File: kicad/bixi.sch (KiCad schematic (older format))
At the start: 20 parts, among them J1 RJ45, J2 RJ45, J3 RJ45, J4 RJ45, J5 RJ45, J6 RJ45, J7 RJ45, J8 RJ45, U1 Teensy3.6, U2 sn75lbc978, U3 ESP8266

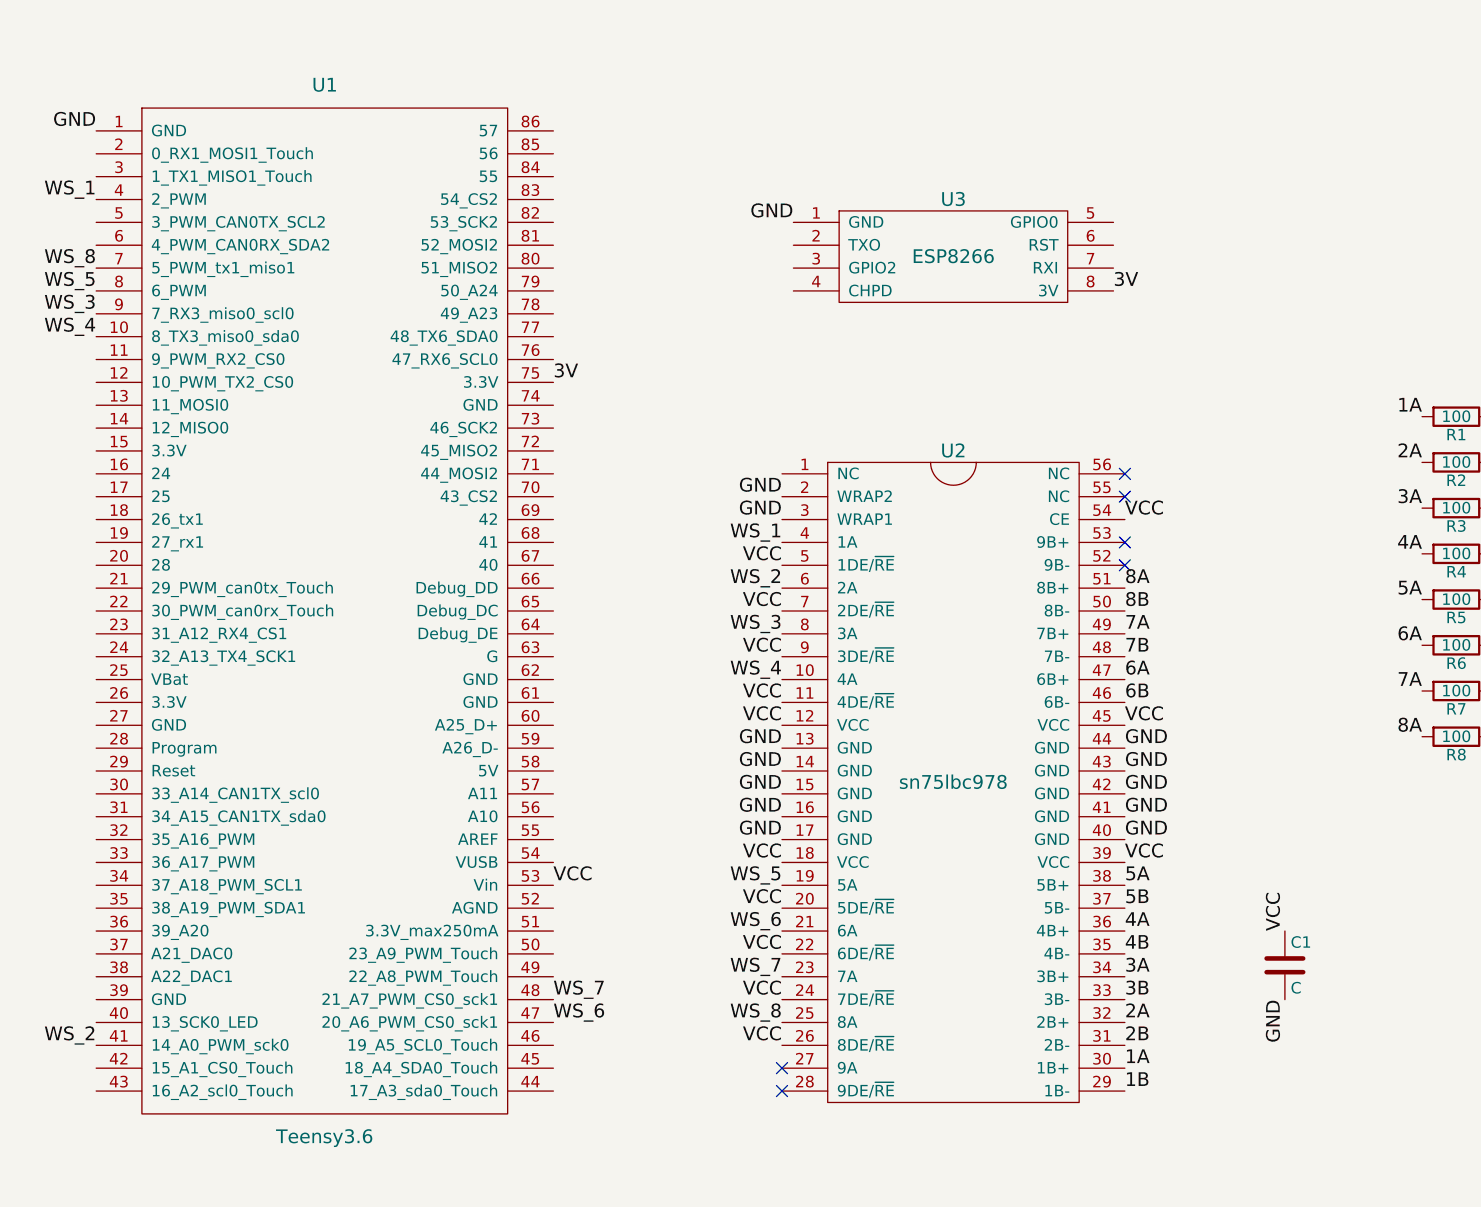
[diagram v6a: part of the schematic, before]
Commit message: v3 boards almost complete. added xcvr breakout, passthrough boards
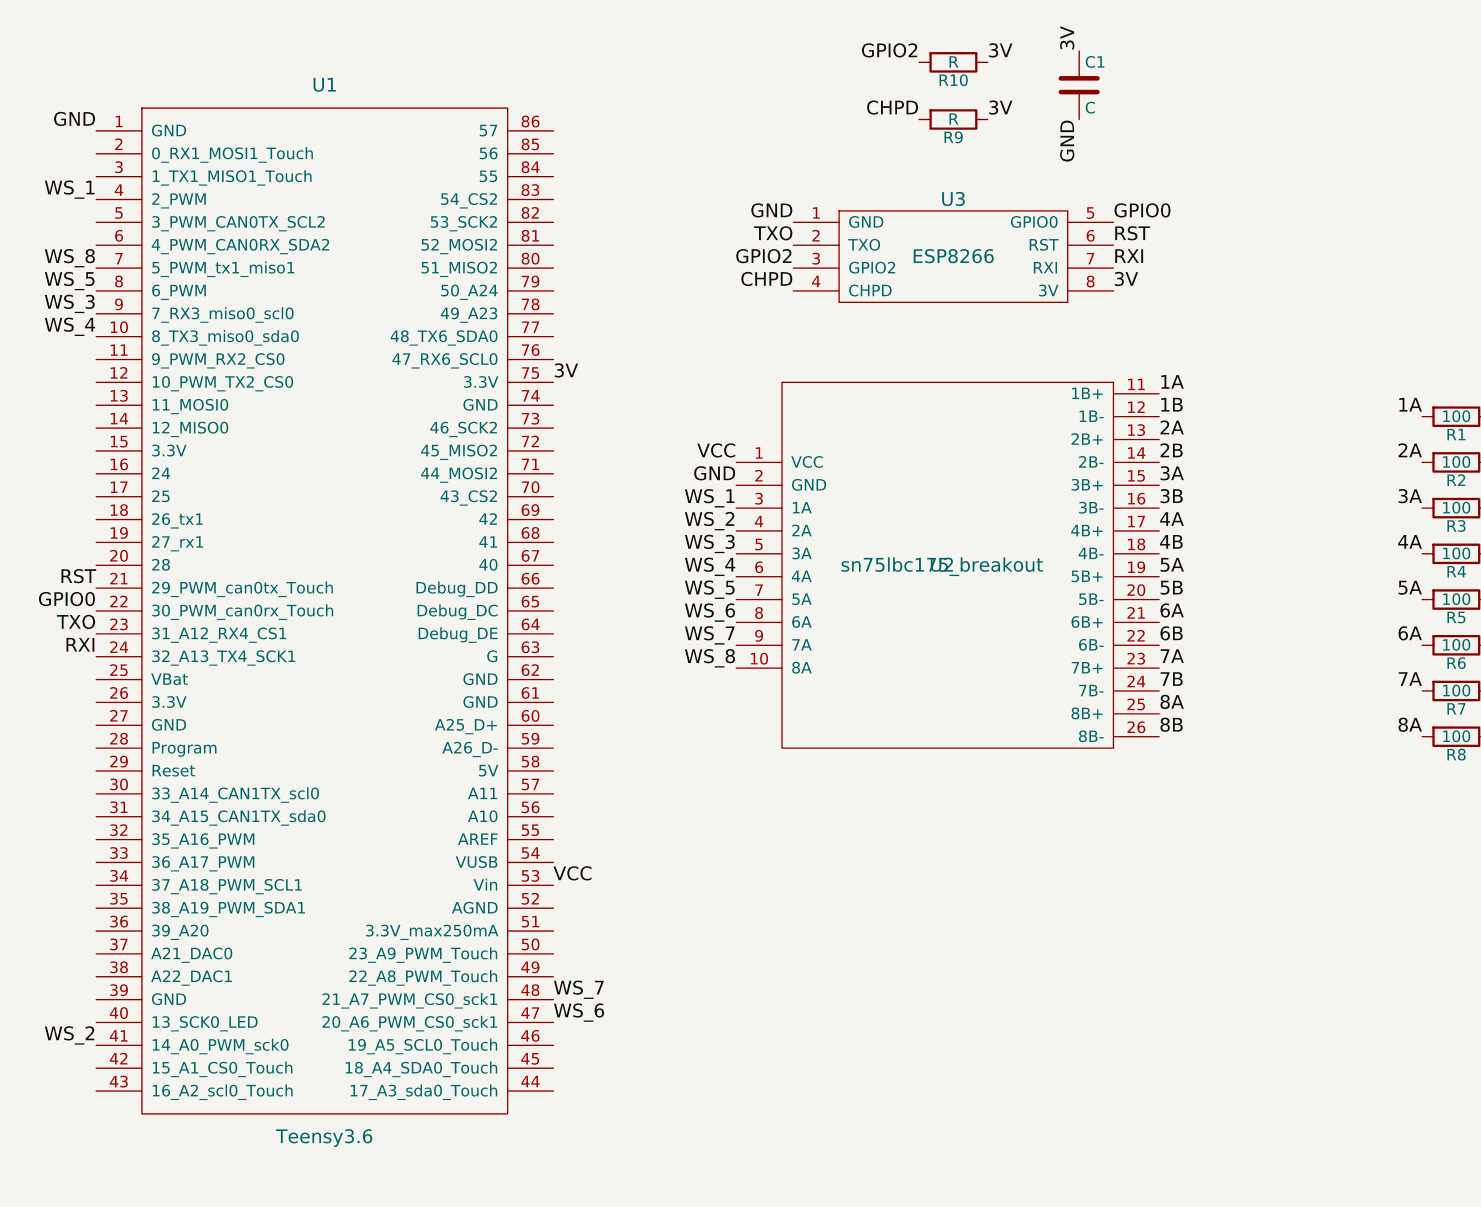
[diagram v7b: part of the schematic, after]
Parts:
- removed U2: sn75lbc978, Housings_SSOP:SSOP-56_7.5x18.5mm_Pitch0.635mm, symbol sn75lbc978
- added R10, R9: R, Resistors_THT:R_Axial_DIN0207_L6.3mm_D2.5mm_P7.62mm_Horizontal, symbol R
- added U2: sn75lbc175_breakout, custom:sn75lbc17f_breakout, symbol sn75lbc175_breakout
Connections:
- net 1A: now also U2.11 (1B+)
- net 1B: now also U2.12 (1B-)
- net 2A: now also U2.13 (2B+)
- net 2B: now also U2.14 (2B-)
- net 3A: now also U2.15 (3B+)
- net 3B: now also U2.16 (3B-)
- net 3V: now also C1.1, R10.1, R9.1
- net 4A: now also U2.17 (4B+)
- net 4B: now also U2.18 (4B-)
- net 5A: now also U2.19 (5B+)
- net 5B: now also U2.20 (5B-)
- net 6A: now also U2.21 (6B+)
- net 6B: now also U2.22 (6B-)
- net 7A: now also U2.23 (7B+)
- net 7B: now also U2.24 (7B-)
- net 8A: now also U2.25 (8B+)
- net 8B: now also U2.26 (8B-)
- net GND: now also U2.2 (GND)
- net VCC: now also U2.1 (VCC); no longer C1.1
- net WS_1: now also U2.3 (1A)
- net WS_2: now also U2.4 (2A)
- net WS_3: now also U2.5 (3A)
- net WS_4: now also U2.6 (4A)
- net WS_5: now also U2.7 (5A)
- net WS_6: now also U2.8 (6A)
- net WS_7: now also U2.9 (7A)
- net WS_8: now also U2.10 (8A)
- net RST: now reaches U1.21 (29_PWM_can0tx_Touch)
- net RST: now also U3.6 (RST)
- net GPIO0: now reaches U1.22 (30_PWM_can0rx_Touch)
- net GPIO0: now also U3.5 (GPIO0)
- net TXO: now reaches U1.23 (31_A12_RX4_CS1)
- net TXO: now also U3.2 (TXO)
- net RXI: now reaches U1.24 (32_A13_TX4_SCK1)
- net RXI: now also U3.7 (RXI)
- net GPIO2: now reaches U3.3 (GPIO2)
- net GPIO2: now also R10.2
- net CHPD: now reaches U3.4 (CHPD)
- net CHPD: now also R9.2
- no-connect marks 6 -> 0
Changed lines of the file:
@@
-	1    0    0    -1
-$EndComp
-$Comp
-L C C1
-U 1 1 58BF16CF
-P 6800 4850
-F 0 "C1" H 6825 4950 50  0000 L CNN
-F 1 "C" H 6825 4750 50  0000 L CNN
-F 2 "Capacitors_THT:C_Disc_D4.7mm_W2.5mm_P5.00mm" H 6838 4700 50  0001 C CNN
-F 3 "" H 6800 4850 50  0000 C CNN
-	1    6800 4850
-	1    0    0    -1
-$EndComp
-$Comp
-L sn75lbc978 U2
-U 1 1 5904BED1
-P 5350 4050
-F 0 "U2" H 5350 5500 60  0000 C CNN
-F 1 "sn75lbc978" H 5350 4050 60  0000 C CNN
-F 2 "Housings_SSOP:SSOP-56_7.5x18.5mm_Pitch0.635mm" H 5350 4050 60  0001 C CNN
-F 3 "" H 5350 4050 60  0001 C CNN
-	1    5350 4050
 	1    0    0    -1
 $EndComp
@@
 Text Label 1600 1500 2    60   ~ 0
 WS_1
-Text Label 4600 3000 2    60   ~ 0
+Text Label 4400 2850 2    60   ~ 0
 WS_1
-Text Label 4600 3200 2    60   ~ 0
+Text Label 4400 2950 2    60   ~ 0
 WS_2
-Text Label 4600 3400 2    60   ~ 0
+Text Label 4400 3050 2    60   ~ 0
 WS_3
-Text Label 4600 3600 2    60   ~ 0
+Text Label 4400 3150 2    60   ~ 0
 WS_4
-Text Label 4600 4500 2    60   ~ 0
+Text Label 4400 3250 2    60   ~ 0
 WS_5
-Text Label 4600 4700 2    60   ~ 0
+Text Label 4400 3350 2    60   ~ 0
 WS_6
-Text Label 4600 4900 2    60   ~ 0
+Text Label 4400 3450 2    60   ~ 0
 WS_7
-Text Label 4600 5100 2    60   ~ 0
+Text Label 4400 3550 2    60   ~ 0
 WS_8
 Text Label 1600 1200 2    60   ~ 0
@@
 Text Label 3600 4500 0    60   ~ 0
 VCC
-Text Label 6100 4400 0    60   ~ 0
+Text Label 4400 2650 2    60   ~ 0
 VCC
-Text Label 6100 3800 0    60   ~ 0
-VCC
-Text Label 4600 3800 2    60   ~ 0
-VCC
-Text Label 4600 4400 2    60   ~ 0
-VCC
-Text Label 4600 3900 2    60   ~ 0
-GND
-Text Label 4600 4000 2    60   ~ 0
-GND
-Text Label 4600 4100 2    60   ~ 0
-GND
-Text Label 4600 4200 2    60   ~ 0
-GND
-Text Label 4600 4300 2    60   ~ 0
-GND
-Text Label 6100 3900 0    60   ~ 0
-GND
-Text Label 6100 4000 0    60   ~ 0
-GND
-Text Label 6100 4100 0    60   ~ 0
-GND
-Text Label 6100 4200 0    60   ~ 0
-GND
-Text Label 6100 4300 0    60   ~ 0
-GND
-Text Label 6100 2900 0    60   ~ 0
-VCC
-Text Label 4600 2800 2    60   ~ 0
-GND
-Text Label 4600 2900 2    60   ~ 0
-GND
-Text Label 4600 3100 2    60   ~ 0
-VCC
-Text Label 4600 3300 2    60   ~ 0
-VCC
-Text Label 4600 3500 2    60   ~ 0
-VCC
-Text Label 4600 3700 2    60   ~ 0
-VCC
-Text Label 4600 4600 2    60   ~ 0
-VCC
-Text Label 4600 4800 2    60   ~ 0
-VCC
-Text Label 4600 5000 2    60   ~ 0
-VCC
-Text Label 4600 5200 2    60   ~ 0
-VCC
-NoConn ~ 4600 5300
-NoConn ~ 4600 5400
-NoConn ~ 6100 2700
-NoConn ~ 6100 2800
-NoConn ~ 6100 3000
-NoConn ~ 6100 3100
-Text Label 6100 5400 0    60   ~ 0
+Text Label 4400 2750 2    60   ~ 0
+GND
+Text Label 6250 2450 0    60   ~ 0
 1B
-Text Label 6100 5300 0    60   ~ 0
+Text Label 6250 2350 0    60   ~ 0
 1A
-Text Label 6100 5200 0    60   ~ 0
+Text Label 6250 2650 0    60   ~ 0
 2B
-Text Label 6100 5100 0    60   ~ 0
+Text Label 6250 2550 0    60   ~ 0
 2A
-Text Label 6100 5000 0    60   ~ 0
+Text Label 6250 2850 0    60   ~ 0
 3B
-Text Label 6100 4900 0    60   ~ 0
+Text Label 6250 2750 0    60   ~ 0
 3A
-Text Label 6100 4800 0    60   ~ 0
+Text Label 6250 3050 0    60   ~ 0
 4B
-Text Label 6100 4700 0    60   ~ 0
+Text Label 6250 2950 0    60   ~ 0
 4A
-Text Label 6100 4600 0    60   ~ 0
+Text Label 6250 3250 0    60   ~ 0
 5B
-Text Label 6100 4500 0    60   ~ 0
+Text Label 6250 3150 0    60   ~ 0
 5A
-Text Label 6100 3700 0    60   ~ 0
+Text Label 6250 3450 0    60   ~ 0
 6B
-Text Label 6100 3600 0    60   ~ 0
+Text Label 6250 3350 0    60   ~ 0
 6A
-Text Label 6100 3500 0    60   ~ 0
+Text Label 6250 3650 0    60   ~ 0
 7B
-Text Label 6100 3400 0    60   ~ 0
+Text Label 6250 3550 0    60   ~ 0
 7A
-Text Label 6100 3300 0    60   ~ 0
+Text Label 6250 3850 0    60   ~ 0
 8B
-Text Label 6100 3200 0    60   ~ 0
+Text Label 6250 3750 0    60   ~ 0
 8A
 Text Label 8750 1850 3    60   ~ 0
@@
 Text Label 7700 3850 0    60   ~ 0
 8B
-Text Label 6800 4700 1    60   ~ 0
-VCC
-Text Label 6800 5000 3    60   ~ 0
-GND
 $Comp
 L ESP8266 U3
@@
 Text Label 3600 2300 0    60   ~ 0
 3V
+$Comp
+L sn75lbc175_breakout U2
+U 1 1 59067D8D
+P 5300 3100
+F 0 "U2" H 5300 3100 60  0000 C CNN
+F 1 "sn75lbc175_breakout" H 5300 3100 60  0000 C CNN
+F 2 "custom:sn75lbc17f_breakout" H 5300 3100 60  0001 C CNN
+F 3 "" H 5300 3100 60  0001 C CNN
+	1    5300 3100
+	1    0    0    -1
+$EndComp
+$Comp
+L R R9
+U 1 1 5907EA94
+P 5350 1150
+F 0 "R9" V 5430 1150 50  0000 C CNN
+F 1 "R" V 5350 1150 50  0000 C CNN
+F 2 "Resistors_THT:R_Axial_DIN0207_L6.3mm_D2.5mm_P7.62mm_Horizontal" V 5280 1150 50  0001 C CNN
+F 3 "" H 5350 1150 50  0001 C CNN
+	1    5350 1150
+	0    1    1    0
+$EndComp
+Text Label 4650 1900 2    60   ~ 0
+CHPD
+Text Label 5200 1150 2    60   ~ 0
+CHPD
+Text Label 5500 1150 0    60   ~ 0
+3V
+Text Label 4650 1700 2    60   ~ 0
+TXO
+Text Label 1600 3400 2    60   ~ 0
+TXO
+$Comp
+L R R10
+U 1 1 5907EE27
+P 5350 900
+F 0 "R10" V 5430 900 50  0000 C CNN
+F 1 "R" V 5350 900 50  0000 C CNN
+F 2 "Resistors_THT:R_Axial_DIN0207_L6.3mm_D2.5mm_P7.62mm_Horizontal" V 5280 900 50  0001 C CNN
+F 3 "" H 5350 900 50  0001 C CNN
+	1    5350 900
+	0    1    1    0
+$EndComp
+Text Label 4650 1800 2    60   ~ 0
+GPIO2
+Text Label 5200 900  2    60   ~ 0
+GPIO2
+Text Label 5500 900  0    60   ~ 0
+3V
+Text Label 6050 1800 0    60   ~ 0
+RXI
+Text Label 1600 3500 2    60   ~ 0
+RXI
+Text Label 6050 1600 0    60   ~ 0
+GPIO0
+Text Label 6050 1700 0    60   ~ 0
+RST
+Text Label 1600 3200 2    60   ~ 0
+RST
+Text Label 1600 3300 2    60   ~ 0
+GPIO0
+$Comp
+L C C1
+U 1 1 5907F490
+P 5900 1000
+F 0 "C1" H 5925 1100 50  0000 L CNN
+F 1 "C" H 5925 900 50  0000 L CNN
+F 2 "Capacitors_THT:C_Disc_D4.7mm_W2.5mm_P5.00mm" H 5938 850 50  0001 C CNN
+F 3 "" H 5900 1000 50  0001 C CNN
+	1    5900 1000
+	1    0    0    -1
+$EndComp
+Text Label 5900 850  1    60   ~ 0
+3V
+Text Label 5900 1150 3    60   ~ 0
+GND
 $EndSCHEMATC

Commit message: first changes for v4 pcb's
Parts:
- removed U2: sn75lbc175_breakout, custom:sn75lbc17f_breakout, symbol sn75lbc175_breakout
- added C1, C2, C3, C4, C5, C6, C7, C8: C, Capacitors_THT:C_Disc_D4.7mm_W2.5mm_P5.00mm, symbol C
- added U1, U2, U3, U4, U5, U6, U7, U8: SP3481CN, Housings_DIP:DIP-8_W7.62mm, symbol SP3481CN
- renumbered C1 to C9, U3 to U10, U1 to U9
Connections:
- net 1A: now also U1.6 (A)
- net 1B: now also U1.7 (B)
- net 2A: now also U2.6 (A)
- net 2B: now also U2.7 (B)
- net 3A: now also U3.6 (A)
- net 3B: now also U3.7 (B)
- net 4A: now also U4.6 (A)
- net 4B: now also U4.7 (B)
- net 5A: now also U5.6 (A)
- net 5B: now also U5.7 (B)
- net 6A: now also U6.6 (A)
- net 6B: now also U6.7 (B)
- net 7A: now also U7.6 (A)
- net 7B: now also U7.7 (B)
- net 8A: now also U8.6 (A)
- net 8B: now also U8.7 (B)
- net GND: now also C1.2, C2.2, C3.2, C4.2, C5.2, C6.2, C7.2, C8.2, U1.5 (GND), U2.5 (GND), U3.5 (GND), U4.5 (GND), U5.5 (GND), U6.5 (GND), U7.5 (GND), U8.5 (GND)
- net VCC: now also C1.1, C2.1, C3.1, C4.1, C5.1, C6.1, C7.1, C8.1, U1.2 (~RE~), U1.3 (DE), U1.8 (VCC), U2.2 (~RE~), U2.3 (DE), U2.8 (VCC), U3.2 (~RE~), U3.3 (DE), U3.8 (VCC), U4.2 (~RE~), U4.3 (DE), U4.8 (VCC), U5.2 (~RE~), U5.3 (DE), U5.8 (VCC), U6.2 (~RE~), U6.3 (DE), U6.8 (VCC), U7.2 (~RE~), U7.3 (DE), U7.8 (VCC), U8.2 (~RE~), U8.3 (DE), U8.8 (VCC)
- net WS_1: now also U1.4 (DI)
- net WS_2: now also U2.4 (DI)
- net WS_3: now also U3.4 (DI)
- net WS_4: now also U4.4 (DI)
- net WS_5: now also U5.4 (DI)
- net WS_6: now also U6.4 (DI)
- net WS_7: now also U7.4 (DI)
- net WS_8: now also U8.4 (DI)
- no-connect marks 0 -> 8
